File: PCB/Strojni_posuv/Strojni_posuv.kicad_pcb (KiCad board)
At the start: 2 copper layers, 170 x 80 mm, 111 parts, among them IC1 TB6600HG, J1 Conn_01x20_Pin, J2 Button_A, J5 POWER, J6 Button_A, Q1 BSS138, Q2 BSS138, Q3 BSS138, Q4 BSS138, Q5 BSS138, Q6 BSS138, Q7 BC847, SW1 SW_DPST_x2, SW2 SW_DPST_x2, SW3 SW_DPST_x2, SW4 SW_DPST_x2, SW5 SW_DPST_x2, U1 STM32F103RBTx, U3 6N137, U4 MIC5365-3.3YC5, U5 6N137, U6 PC817, U7 74HC14, Y1 16MHz

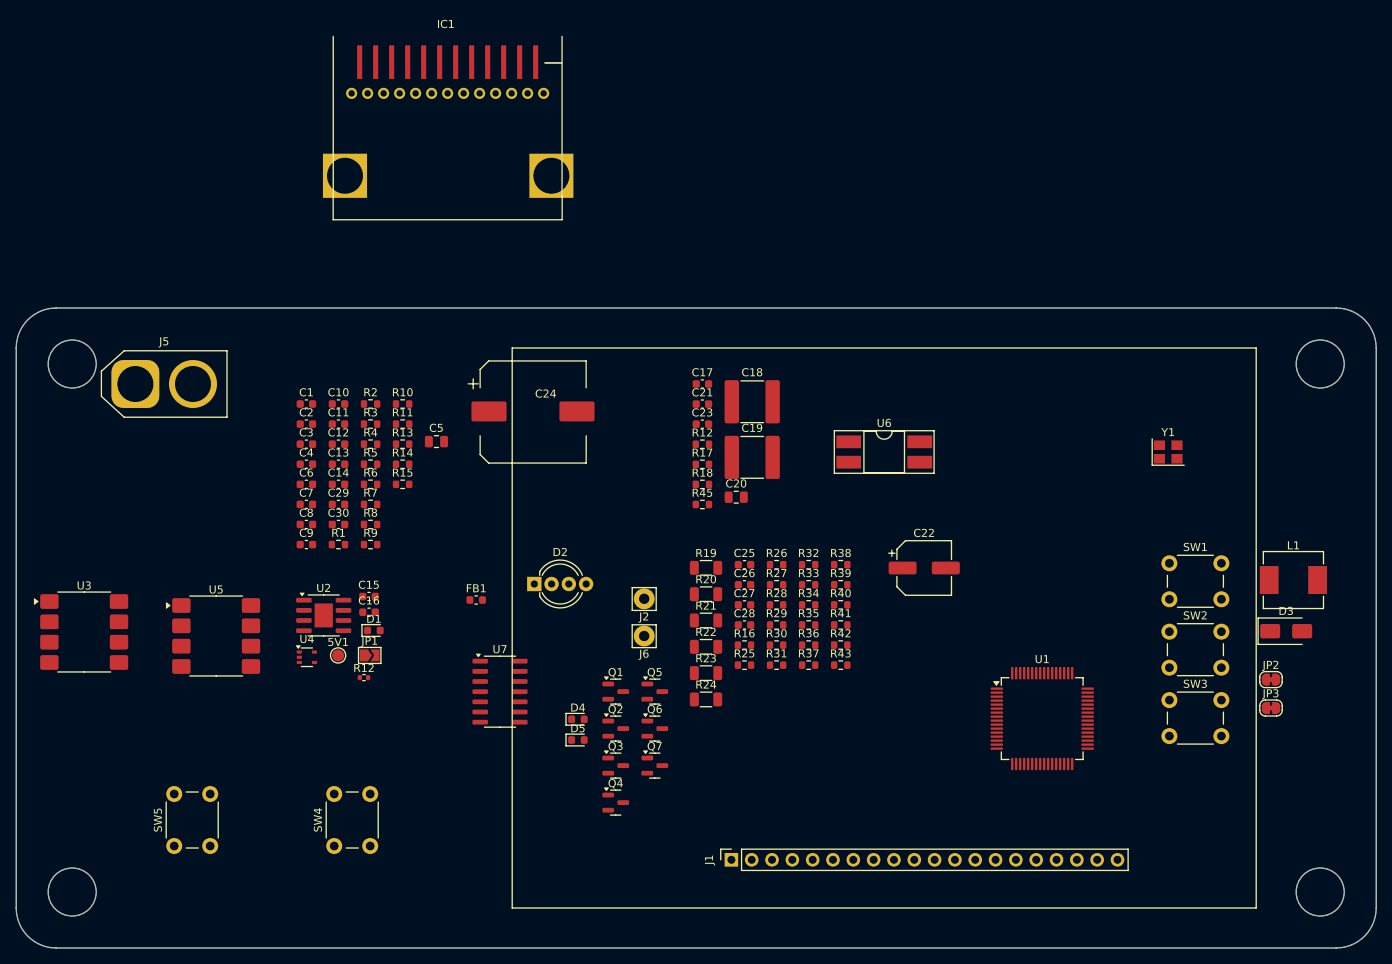
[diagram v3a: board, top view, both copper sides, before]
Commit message: PCB making #6 Placing all components - component layout
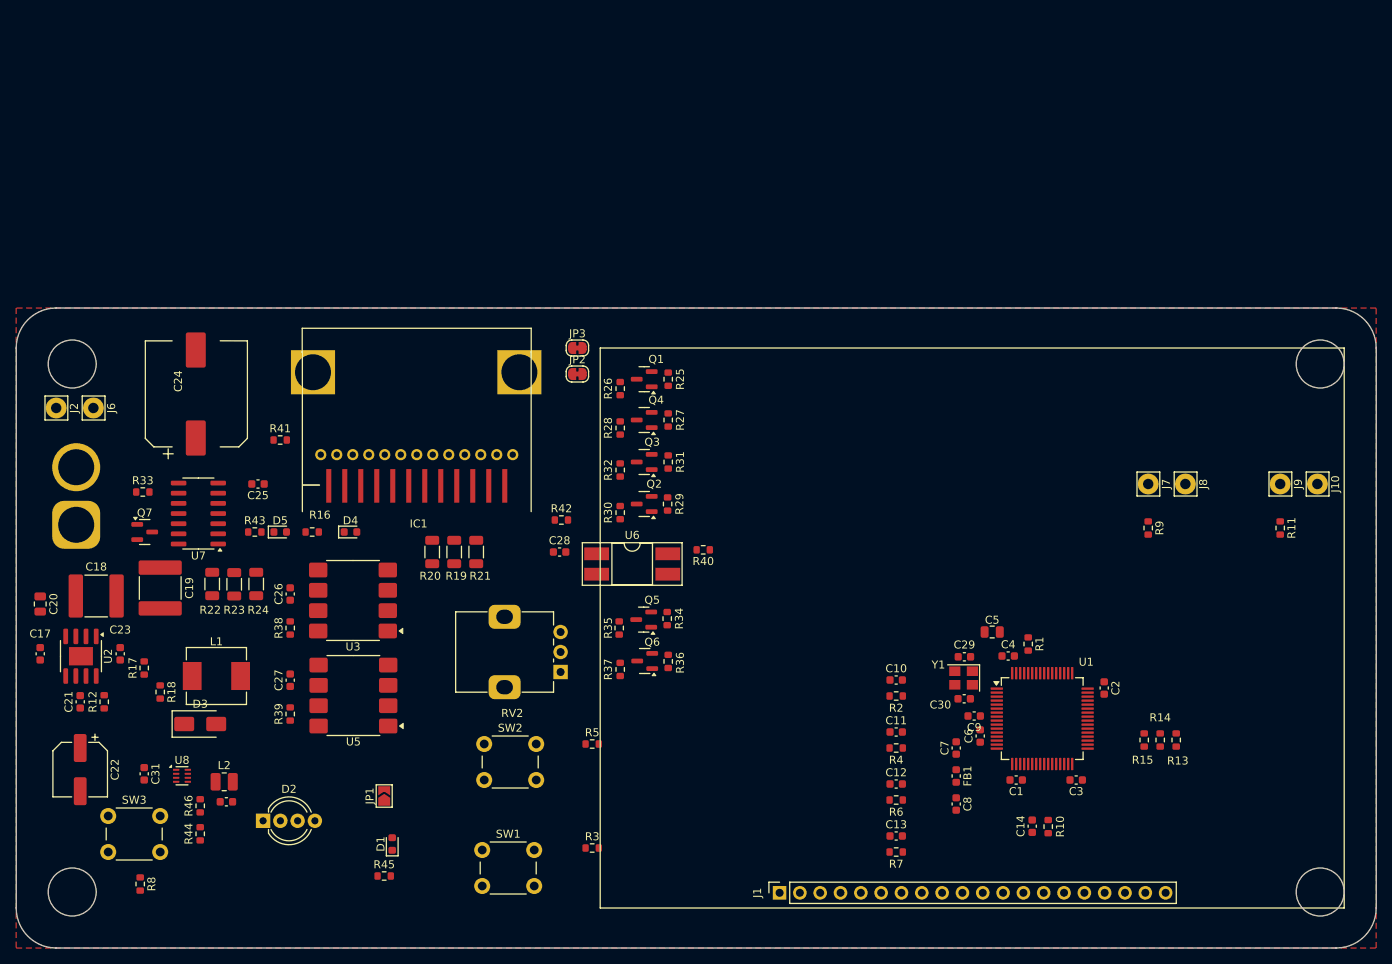
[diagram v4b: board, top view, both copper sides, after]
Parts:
- removed 5V1: 5V, TestPoint:TestPoint_Pad_D1.5mm
- removed C15, C16: 1u, Capacitor_SMD:C_0603_1608Metric
- removed the R12 at (93.5, 76.2)
- removed SW4, SW5: SW_DPST_x2, Button_Switch_THT:SW_PUSH_6mm
- removed U4: MIC5365-3.3YC5, Package_TO_SOT_SMD:SOT-353_SC-70-5
- added C31: 4.7uF, Capacitor_SMD:C_0603_1608Metric, F.Cu at (66.0, 88.2)
- added C32: 10uF, Capacitor_SMD:C_0603_1608Metric, F.Cu at (76.3, 91.7)
- added J10: Button_right_B, Connector_Pin:Pin_D1.3mm_L11.3mm_W2.8mm_Flat, F.Cu at (212.7, 52.0)
- added J7: Button_left_A, Connector_Pin:Pin_D1.3mm_L11.3mm_W2.8mm_Flat, F.Cu at (191.5, 52.0)
- added J8: Button_left_B, Connector_Pin:Pin_D1.3mm_L11.3mm_W2.8mm_Flat, F.Cu at (196.2, 52.0)
- added J9: Button_right_A, Connector_Pin:Pin_D1.3mm_L11.3mm_W2.8mm_Flat, F.Cu at (208.0, 52.0)
- added L2: 470nH-2A, Inductor_SMD:L_1008_2520Metric, F.Cu at (76.0, 89.2)
- added R44: 45.3k, Resistor_SMD:R_0603_1608Metric, F.Cu at (73.0, 95.7)
- added R46: 10k, Resistor_SMD:R_0603_1608Metric, F.Cu at (73.0, 92.2)
- added RV2: R_Potentiometer_10k, Potentiometer_THT:Potentiometer_Alps_RK09K_Single_Vertical, F.Cu at (118.0, 75.5)
- added U8: TPS62822DLC, Package_SON:Texas_VSON-HR-8_1.5x2mm_P0.5mm, F.Cu at (70.7, 88.5)
- J2: value Button_A -> Button_power_A
- J5: moved to B.Cu
- J6: value Button_A -> Button_power_B
- moved D3 136.2 mm to (73.0, 82.0)
- moved L1 135.2 mm to (75.0, 76.0)
- moved SW3 133.4 mm to (61.5, 93.5)
- moved R11 110.5 mm to (208.0, 57.5), turned to -90 degrees
- moved C22 108.5 mm to (58.0, 87.7), turned to -90 degrees
- moved C2 105.0 mm to (186.0, 77.5), turned to -90 degrees
- moved C3 105.0 mm to (182.5, 89.0), turned to 180 degrees
- moved R13 103.5 mm to (195.0, 84.0), turned to 90 degrees
- moved R14 100.8 mm to (193.0, 84.0), turned to 90 degrees
- moved C1 100.4 mm to (175.0, 89.0), turned to 180 degrees
- moved R15 98.1 mm to (191.0, 84.0), turned to 90 degrees
- moved JP3 97.7 mm to (120.2, 35.0)
- moved R9 97.2 mm to (191.5, 57.5), turned to -90 degrees
- moved C14 96.7 mm to (177.0, 94.8), turned to 90 degrees
- moved R10 96.4 mm to (179.0, 94.8), turned to 90 degrees
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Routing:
- added copper zone on F.Cu, net GND

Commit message: New materials + Schuzka
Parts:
- IC1: moved to B.Cu
- moved IC1 2.14 mm to (98.9, 51.0), turned to 0 degrees

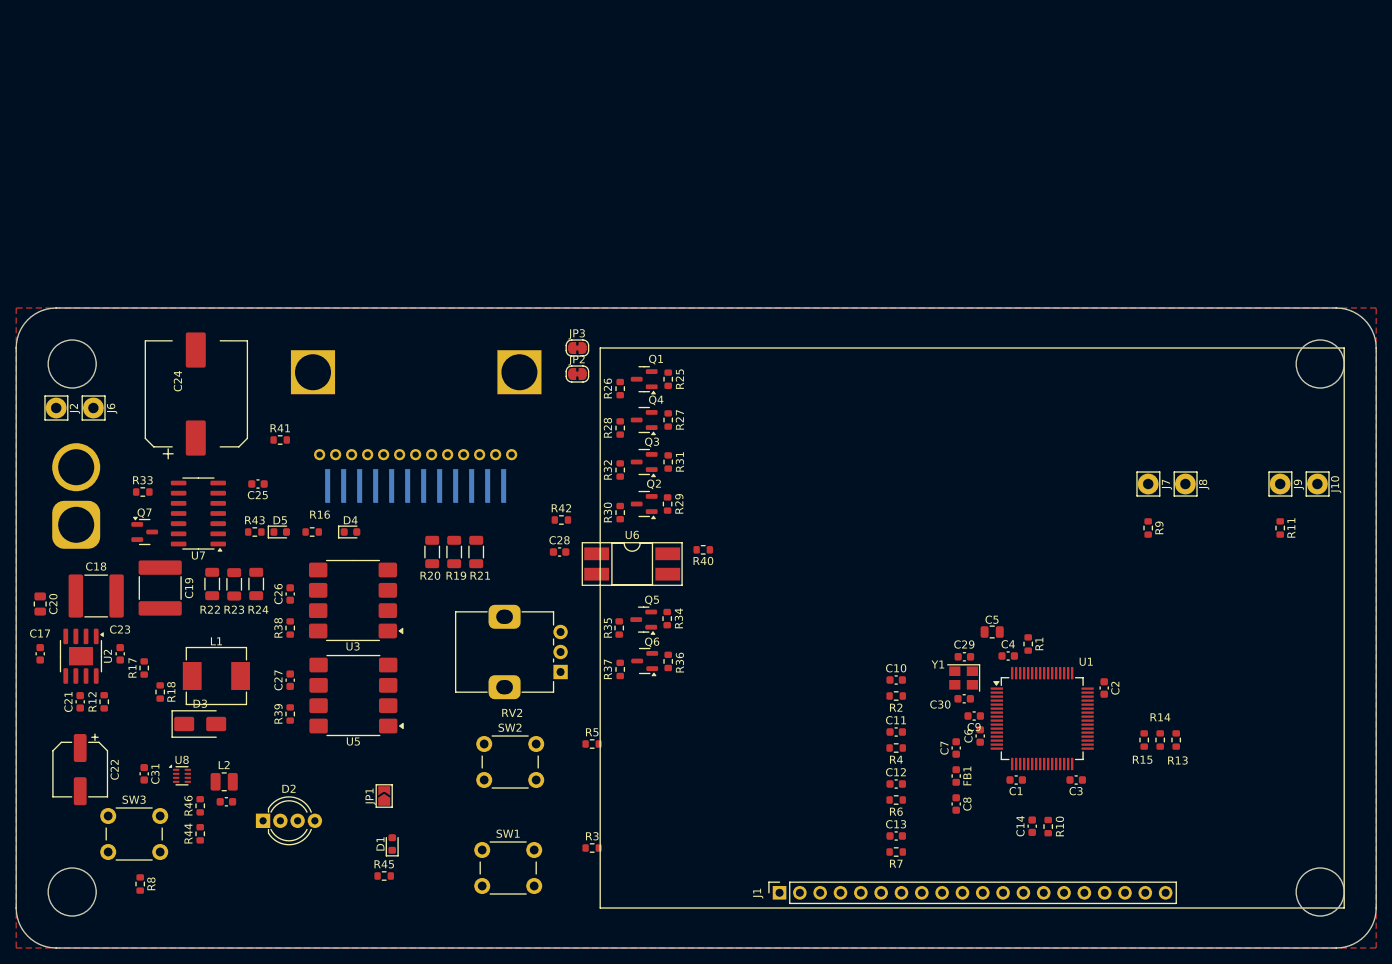
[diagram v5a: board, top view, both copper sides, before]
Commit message: New chapter of PCB making #1
the grind continuesmkdir Useful_materials. redundant systems for 5V logic shifting. 2. rotary encoder. 3. new buttons. 4. placement of components (it is not completed)
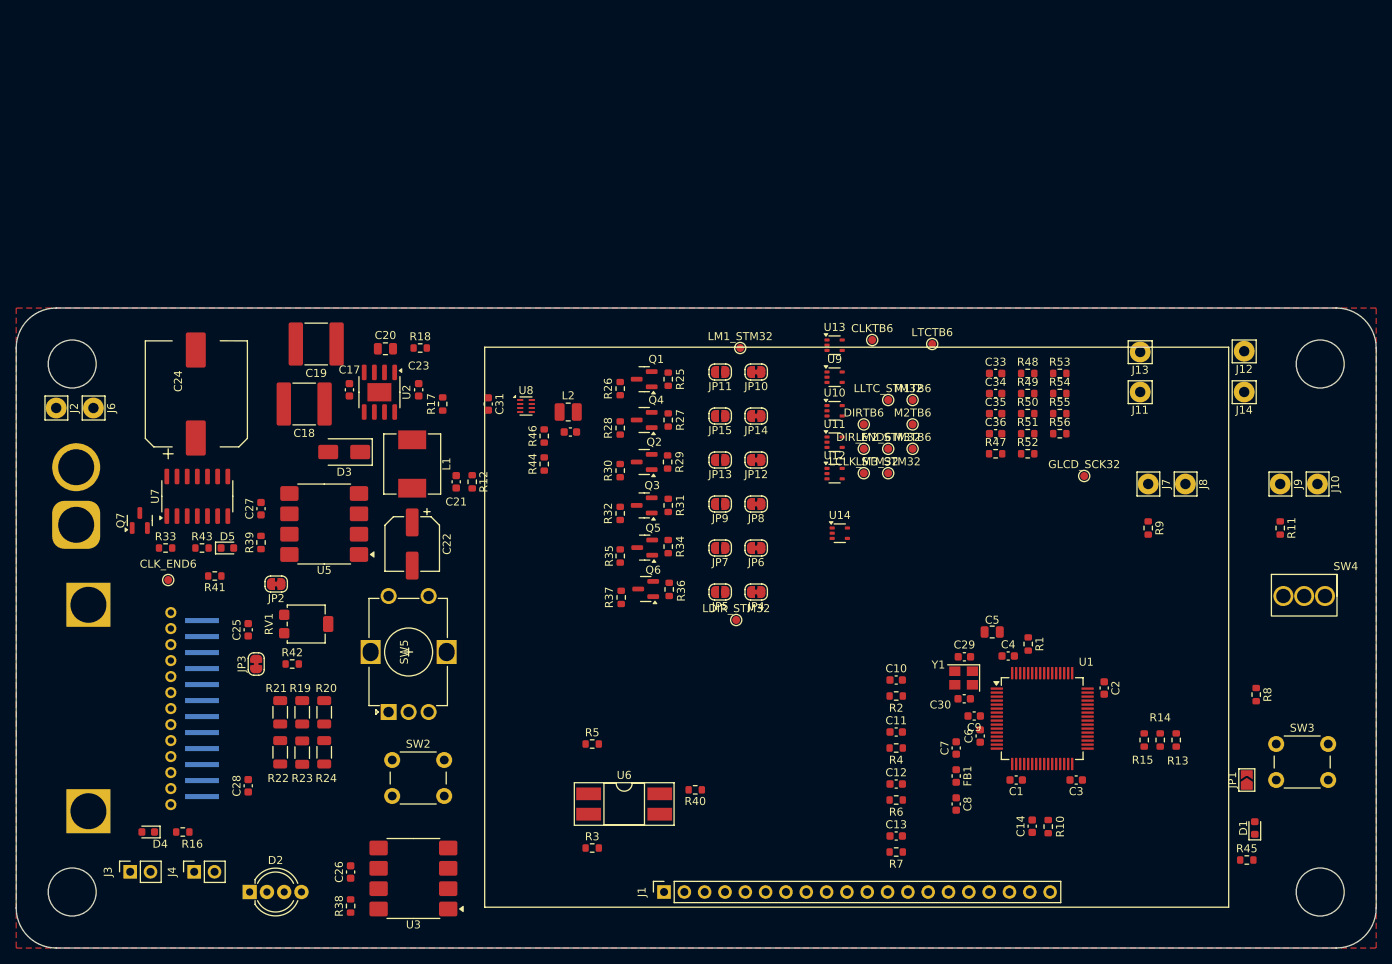
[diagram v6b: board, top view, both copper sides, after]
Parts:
- removed RV2: R_Potentiometer_10k, Potentiometer_THT:Potentiometer_Alps_RK09K_Single_Vertical
- removed SW1: SW_DPST_x2, Button_Switch_THT:SW_PUSH_6mm
- added C33: 100n, Capacitor_SMD:C_0603_1608Metric, F.Cu at (172.4, 38.2)
- added C34: 100n, Capacitor_SMD:C_0603_1608Metric, F.Cu at (172.4, 40.7)
- added C35: 100n, Capacitor_SMD:C_0603_1608Metric, F.Cu at (172.4, 43.2)
- added C36: 100n, Capacitor_SMD:C_0603_1608Metric, F.Cu at (172.4, 45.7)
- added CLKTB6: ~, TestPoint:TestPoint_Pad_D1.0mm, F.Cu at (157.0, 34.0)
- added CLK_END6: ~, TestPoint:TestPoint_Pad_D1.0mm, F.Cu at (69.0, 64.0)
- added DIRTB6: ~, TestPoint:TestPoint_Pad_D1.0mm, F.Cu at (155.9, 44.5)
- added DIR_END6: ~, TestPoint:TestPoint_Pad_D1.0mm, F.Cu at (155.9, 47.6)
- added GLCD_SCK32: ~, TestPoint:TestPoint_Pad_D1.0mm, F.Cu at (183.5, 51.0)
- added J11: Button_left_A, Connector_Pin:Pin_D1.3mm_L11.3mm_W2.8mm_Flat, F.Cu at (190.5, 40.5)
- added J12: Button_right_A, Connector_Pin:Pin_D1.3mm_L11.3mm_W2.8mm_Flat, F.Cu at (203.5, 35.4)
- added J13: Button_left_B, Connector_Pin:Pin_D1.3mm_L11.3mm_W2.8mm_Flat, F.Cu at (190.5, 35.5)
- added J14: Button_right_A, Connector_Pin:Pin_D1.3mm_L11.3mm_W2.8mm_Flat, F.Cu at (203.5, 40.5)
- added J3: OUT1, Connector_PinSocket_2.54mm:PinSocket_1x02_P2.54mm_Vertical, F.Cu at (64.2, 100.5)
- added J4: OUT2, Connector_PinSocket_2.54mm:PinSocket_1x02_P2.54mm_Vertical, F.Cu at (72.2, 100.5)
- added JP10: SolderJumper_2_Bridged, Jumper:SolderJumper-2_P1.3mm_Bridged_RoundedPad1.0x1.5mm, F.Cu at (142.5, 38.0)
- added JP11: SolderJumper_2_Open, Jumper:SolderJumper-2_P1.3mm_Open_RoundedPad1.0x1.5mm, F.Cu at (138.0, 38.0)
- added JP12: SolderJumper_2_Bridged, Jumper:SolderJumper-2_P1.3mm_Bridged_RoundedPad1.0x1.5mm, F.Cu at (142.5, 49.0)
- added JP13: SolderJumper_2_Open, Jumper:SolderJumper-2_P1.3mm_Open_RoundedPad1.0x1.5mm, F.Cu at (138.0, 49.0)
- added JP14: SolderJumper_2_Bridged, Jumper:SolderJumper-2_P1.3mm_Bridged_RoundedPad1.0x1.5mm, F.Cu at (142.5, 43.5)
- added JP15: SolderJumper_2_Open, Jumper:SolderJumper-2_P1.3mm_Open_RoundedPad1.0x1.5mm, F.Cu at (138.0, 43.5)
- added JP4: SolderJumper_2_Bridged, Jumper:SolderJumper-2_P1.3mm_Bridged_RoundedPad1.0x1.5mm, F.Cu at (142.5, 65.5)
- added JP5: SolderJumper_2_Open, Jumper:SolderJumper-2_P1.3mm_Open_RoundedPad1.0x1.5mm, F.Cu at (138.0, 65.5)
- added JP6: SolderJumper_2_Bridged, Jumper:SolderJumper-2_P1.3mm_Bridged_RoundedPad1.0x1.5mm, F.Cu at (142.5, 60.0)
- added JP7: SolderJumper_2_Open, Jumper:SolderJumper-2_P1.3mm_Open_RoundedPad1.0x1.5mm, F.Cu at (138.0, 60.0)
- added JP8: SolderJumper_2_Bridged, Jumper:SolderJumper-2_P1.3mm_Bridged_RoundedPad1.0x1.5mm, F.Cu at (142.5, 54.5)
- added JP9: SolderJumper_2_Open, Jumper:SolderJumper-2_P1.3mm_Open_RoundedPad1.0x1.5mm, F.Cu at (138.0, 54.5)
- added LCLK_STM32: ~, TestPoint:TestPoint_Pad_D1.0mm, F.Cu at (155.9, 50.6)
- added LDIR_STM32: ~, TestPoint:TestPoint_Pad_D1.0mm, F.Cu at (140.0, 69.0)
- added LLTC_STM32: ~, TestPoint:TestPoint_Pad_D1.0mm, F.Cu at (159.0, 41.5)
- added LM1_STM32: ~, TestPoint:TestPoint_Pad_D1.0mm, F.Cu at (140.5, 35.0)
- added LM2_STM32: ~, TestPoint:TestPoint_Pad_D1.0mm, F.Cu at (159.0, 47.6)
- added LM3_STM32: ~, TestPoint:TestPoint_Pad_D1.0mm, F.Cu at (159.0, 50.6)
- added LTCTB6: ~, TestPoint:TestPoint_Pad_D1.0mm, F.Cu at (164.5, 34.5)
- added M1TB6: ~, TestPoint:TestPoint_Pad_D1.0mm, F.Cu at (162.1, 41.5)
- added M2TB6: ~, TestPoint:TestPoint_Pad_D1.0mm, F.Cu at (162.1, 44.5)
- added M3TB6: ~, TestPoint:TestPoint_Pad_D1.0mm, F.Cu at (162.1, 47.6)
- added R47: 10K, Resistor_SMD:R_0603_1608Metric, F.Cu at (172.4, 48.2)
- added R48: 10K, Resistor_SMD:R_0603_1608Metric, F.Cu at (176.4, 38.2)
- added R49: 16.5K, Resistor_SMD:R_0603_1608Metric, F.Cu at (176.4, 40.7)
- added R50: 16.5K, Resistor_SMD:R_0603_1608Metric, F.Cu at (176.4, 43.2)
- added R51: 470, Resistor_SMD:R_0603_1608Metric, F.Cu at (176.4, 45.7)
- added R52: 470, Resistor_SMD:R_0603_1608Metric, F.Cu at (176.4, 48.2)
- added R53: 16.5K, Resistor_SMD:R_0603_1608Metric, F.Cu at (180.4, 38.2)
- added R54: 470, Resistor_SMD:R_0603_1608Metric, F.Cu at (180.4, 40.7)
- added R55: 16.5K, Resistor_SMD:R_0603_1608Metric, F.Cu at (180.4, 43.2)
- added R56: 470, Resistor_SMD:R_0603_1608Metric, F.Cu at (180.4, 45.7)
- added RV1: 10K PRESET, Potentiometer_SMD:Potentiometer_Bourns_3314G_Vertical, F.Cu at (86.2, 69.5)
- added SW4: SW_SPDT, Three_way_switch:On-On, F.Cu at (211.0, 66.0)
- added SW5: RotaryEncoder_Switch, Encoder:Rotary_encoder_GME, F.Cu at (99.0, 73.0)
- added U10: 74AHCT1G125, Package_TO_SOT_SMD:SOT-353_SC-70-5, F.Cu at (152.3, 42.9)
- added U11: 74AHCT1G125, Package_TO_SOT_SMD:SOT-353_SC-70-5, F.Cu at (152.3, 46.8)
- added U12: 74AHCT1G125, Package_TO_SOT_SMD:SOT-353_SC-70-5, F.Cu at (152.3, 50.7)
- added U13: 74AHCT1G125, Package_TO_SOT_SMD:SOT-353_SC-70-5, F.Cu at (152.3, 34.6)
- added U14: 74AHCT1G125, Package_TO_SOT_SMD:SOT-353_SC-70-5, F.Cu at (152.9, 58.1)
- added U9: 74AHCT1G125, Package_TO_SOT_SMD:SOT-353_SC-70-5, F.Cu at (152.3, 38.6)
- J10: value Button_right_B -> Button_right_A
- moved SW3 146.3 mm to (207.5, 84.5)
- moved R8 141.5 mm to (205.0, 78.3)
- moved D1 107.8 mm to (204.8, 95.0)
- moved JP1 107.8 mm to (203.8, 89.0)
- moved R45 107.8 mm to (203.8, 99.0)
- moved C31 63.1 mm to (109.0, 42.0)
- moved C32 63.1 mm to (119.3, 45.5)
- moved L2 63.1 mm to (119.0, 43.0)
- moved R44 63.1 mm to (116.0, 49.5)
- moved R46 63.1 mm to (116.0, 46.0)
- moved U8 63.1 mm to (113.7, 42.2)
- moved JP3 56.3 mm to (80.0, 74.5), turned to 90 degrees
- moved C21 54.5 mm to (105.0, 51.7), turned to -90 degrees
- moved R18 53.9 mm to (100.5, 35.0), turned to 0 degrees
- moved C20 53.7 mm to (96.2, 35.1), turned to 0 degrees
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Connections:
- C10 pad 2: Button_conf -> Net-(C10-Pad2)
- Q1 pad 2: M1_STM -> Net-(JP11-B)
- Q2 pad 2: M3_STM -> Net-(JP13-B)
- Q3 pad 2: LTC_STM -> Net-(JP9-B)
- Q4 pad 2: M2_STM -> Net-(JP15-B)
- Q5 pad 2: STEP_STM -> Net-(JP7-B)
- Q6 pad 2: DIR_STM -> Net-(JP5-B)
- R2 pad 2: Button_conf -> Net-(C10-Pad2)
- R25 pad 1: M1_STM -> Net-(JP11-B)
- R27 pad 1: M2_STM -> Net-(JP15-B)
- R29 pad 1: M3_STM -> Net-(JP13-B)
- R3 pad 1: Net-(SW1A-A) -> Button_encoder
- R3 pad 2: Button_conf -> Net-(C10-Pad2)
- R31 pad 1: LTC_STM -> Net-(JP9-B)
- R34 pad 1: STEP_STM -> Net-(JP7-B)
- R36 pad 1: DIR_STM -> Net-(JP5-B)
- U1 pad 25: unconnected-(U1-PC5-Pad25) -> Button_left_fast
- U1 pad 27: unconnected-(U1-PB1-Pad27) -> Right
- U1 pad 28: unconnected-(U1-PB2-Pad28) -> Left
- U1 pad 37: unconnected-(U1-PC6-Pad37) -> Button_right_fast
- U1 pad 43: unconnected-(U1-PA10-Pad43) -> Enc_CLK
- U1 pad 44: unconnected-(U1-PA11-Pad44) -> Enc_DT
- U1 pad 9: Button_prec -> Button_encoder

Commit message: New chapter of PCB making #2
pcb placement
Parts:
- J11: value Button_left_A -> Button_left_fast_A
- J12: value Button_right_A -> Button_right_fast_A
- J13: value Button_left_B -> Button_left_fast_B
- J14: value Button_right_A -> Button_right_fast_B
- moved R48 82.4 mm to (107.2, 83.0)
- moved DIR_END6 81.0 mm to (91.2, 96.2)
- moved R47 72.0 mm to (107.2, 78.8), turned to 180 degrees
- moved GLCD_SCK32 51.4 mm to (166.5, 99.5)
- moved C11 49.7 mm to (110.5, 87.2)
- moved R4 49.7 mm to (110.5, 89.2)
- moved C14 49.3 mm to (202.0, 52.3), turned to -90 degrees
- moved C36 48.1 mm to (212.2, 72.8), turned to 180 degrees
- moved C13 48.0 mm to (180.2, 52.5)
- moved R7 48.0 mm to (180.2, 54.5)
- moved R6 47.9 mm to (205.8, 77.2), turned to 180 degrees
- moved R10 47.5 mm to (200.0, 52.2), turned to -90 degrees
- moved C12 46.9 mm to (205.8, 79.2), turned to 180 degrees
- moved R55 44.6 mm to (212.2, 74.5), turned to 180 degrees
- moved C10 42.7 mm to (117.3, 75.0)
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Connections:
- C35 pad 2: Net-(SW4-A) -> Left
- C36 pad 2: Net-(SW4-C) -> Right
- R53 pad 2: Net-(SW4-A) -> Left
- R55 pad 2: Net-(SW4-C) -> Right
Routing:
- added copper zone on B.Cu, net GND
